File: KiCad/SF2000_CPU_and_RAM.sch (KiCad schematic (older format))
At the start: 5 parts, among them U10 IS61WV20488FBLL-10TLI, U11 IS61WV20488FBLL-10TLI, U12 IS61WV20488FBLL-10TLI, U8 68000D, U9 IS61WV20488FBLL-10TLI

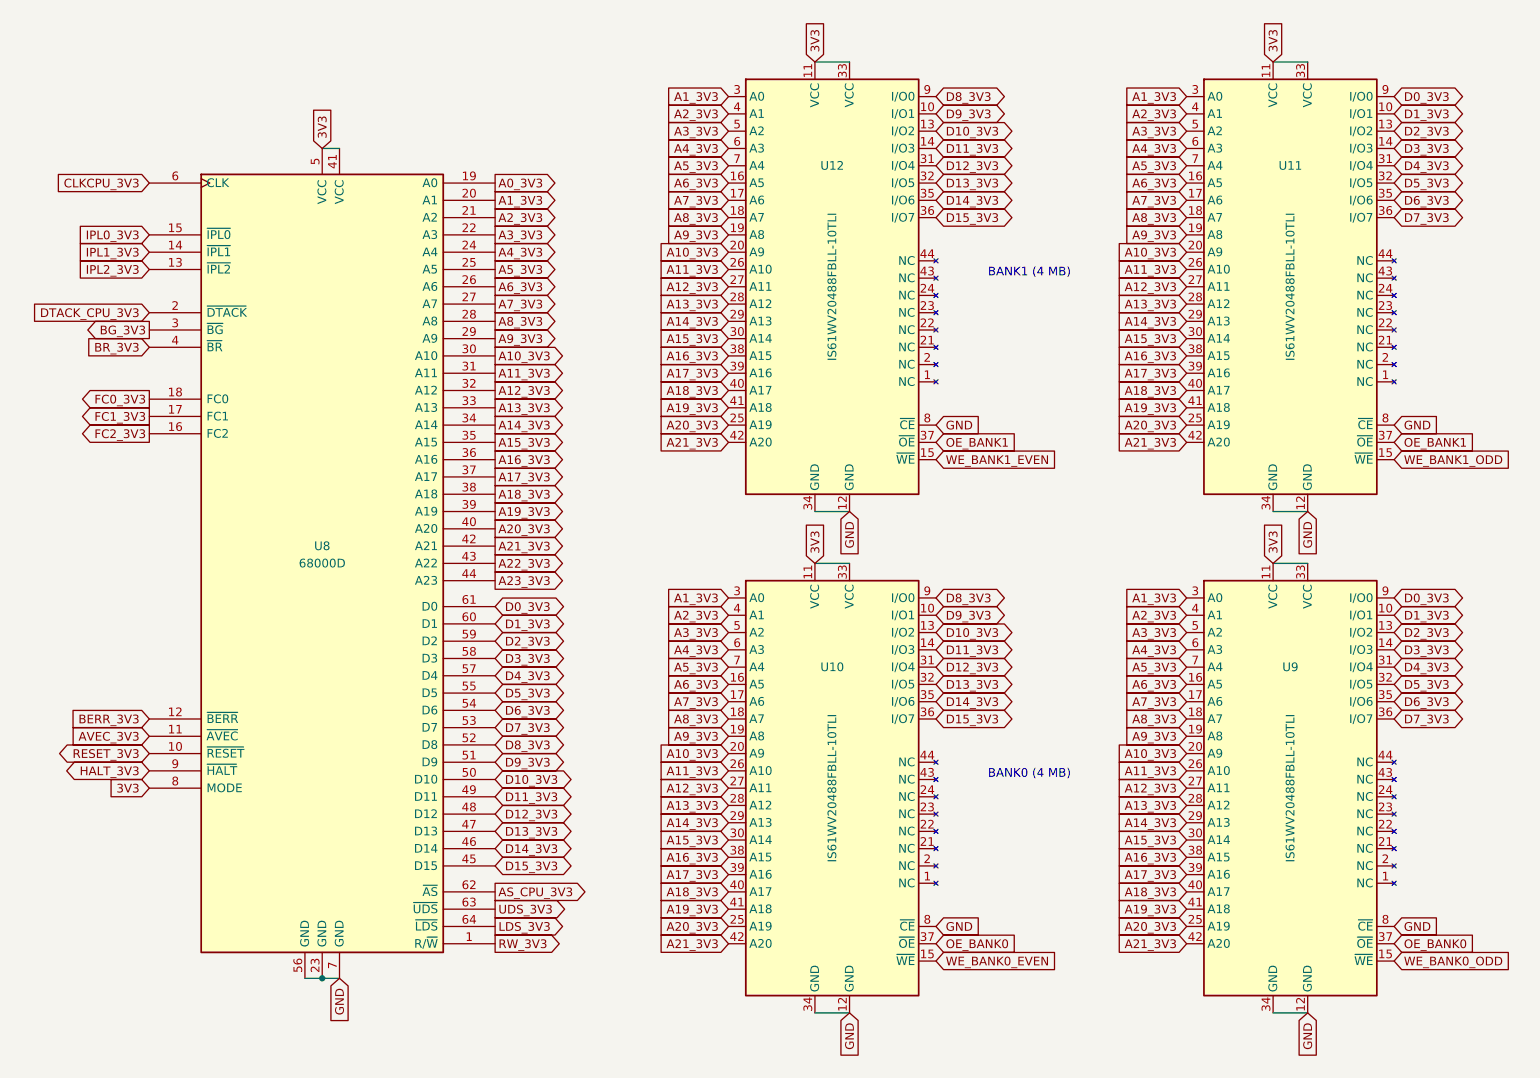
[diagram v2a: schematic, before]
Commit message: rotated SRAM footprints and routed a lot
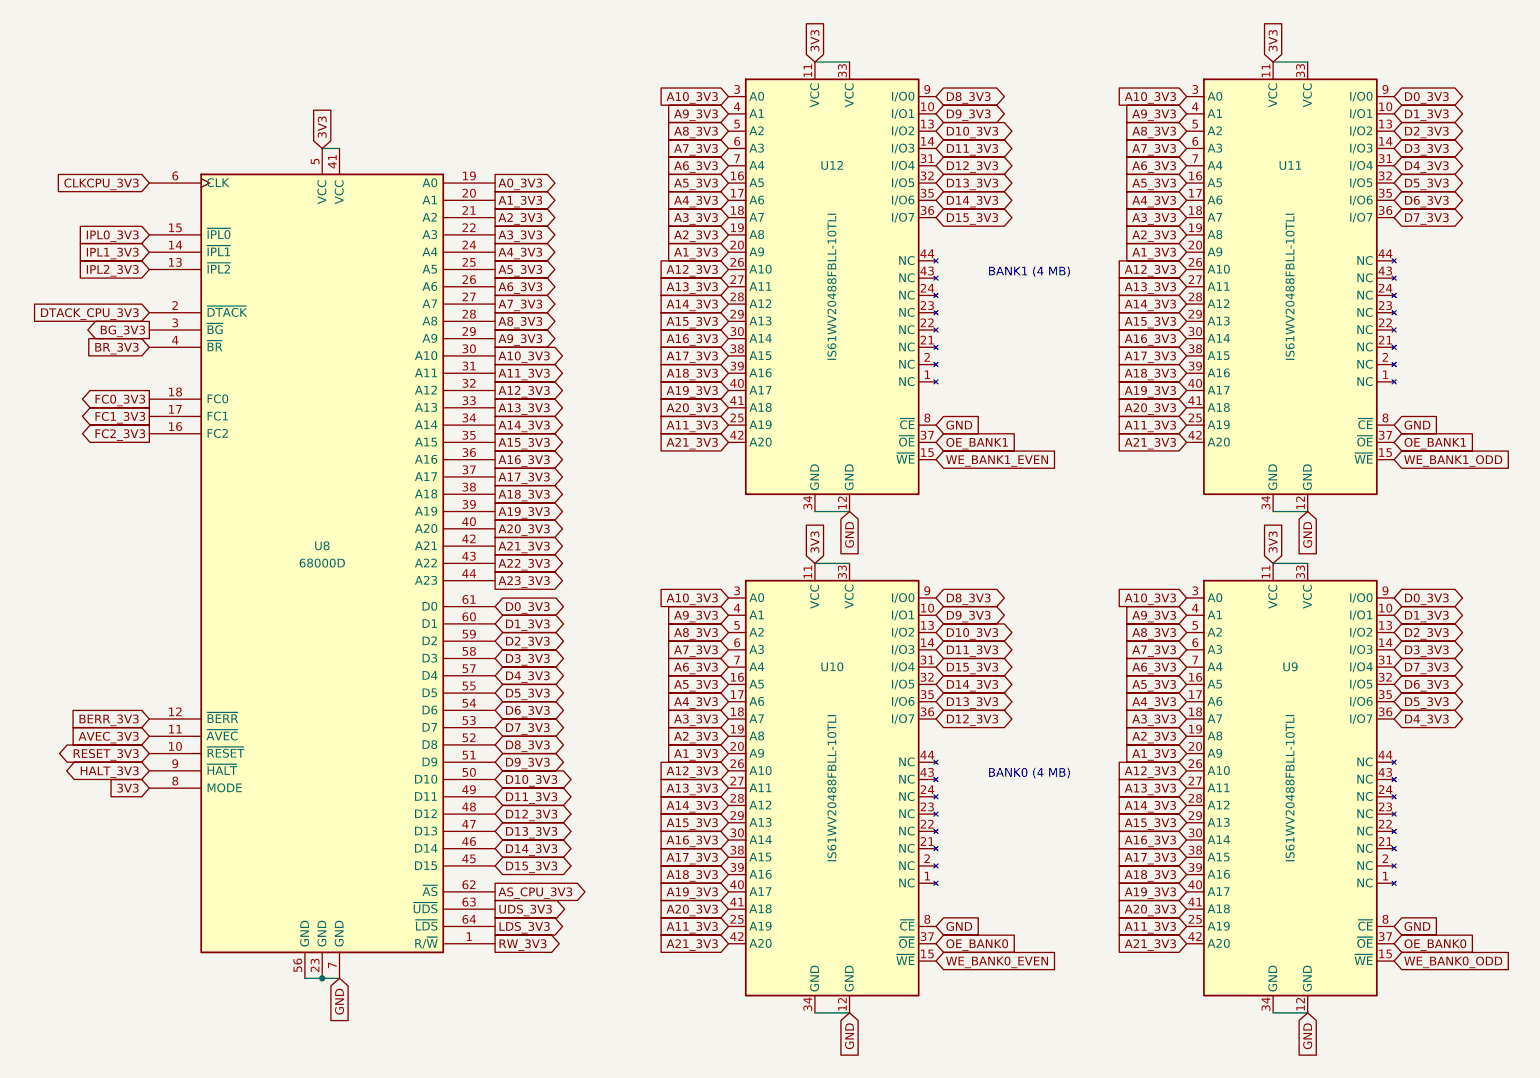
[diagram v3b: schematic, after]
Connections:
- net A10_3V3: now also U10.3 (A0), U11.3 (A0), U12.3 (A0), U9.3 (A0); no longer U10.20 (A9), U11.20 (A9), U12.20 (A9), U9.20 (A9)
- net A11_3V3: now also U10.25 (A19), U11.25 (A19), U12.25 (A19), U9.25 (A19); no longer U10.26 (A10), U11.26 (A10), U12.26 (A10), U9.26 (A10)
- net A12_3V3: now also U10.26 (A10), U11.26 (A10), U12.26 (A10), U9.26 (A10); no longer U10.27 (A11), U11.27 (A11), U12.27 (A11), U9.27 (A11)
- net A13_3V3: now also U10.27 (A11), U11.27 (A11), U12.27 (A11), U9.27 (A11); no longer U10.28 (A12), U11.28 (A12), U12.28 (A12), U9.28 (A12)
- net A14_3V3: now also U10.28 (A12), U11.28 (A12), U12.28 (A12), U9.28 (A12); no longer U10.29 (A13), U11.29 (A13), U12.29 (A13), U9.29 (A13)
- net A15_3V3: now also U10.29 (A13), U11.29 (A13), U12.29 (A13), U9.29 (A13); no longer U10.30 (A14), U11.30 (A14), U12.30 (A14), U9.30 (A14)
- net A16_3V3: now also U10.30 (A14), U11.30 (A14), U12.30 (A14), U9.30 (A14); no longer U10.38 (A15), U11.38 (A15), U12.38 (A15), U9.38 (A15)
- net A17_3V3: now also U10.38 (A15), U11.38 (A15), U12.38 (A15), U9.38 (A15); no longer U10.39 (A16), U11.39 (A16), U12.39 (A16), U9.39 (A16)
- net A18_3V3: now also U10.39 (A16), U11.39 (A16), U12.39 (A16), U9.39 (A16); no longer U10.40 (A17), U11.40 (A17), U12.40 (A17), U9.40 (A17)
- net A19_3V3: now also U10.40 (A17), U11.40 (A17), U12.40 (A17), U9.40 (A17); no longer U10.41 (A18), U11.41 (A18), U12.41 (A18), U9.41 (A18)
- net A1_3V3: now also U10.20 (A9), U11.20 (A9), U12.20 (A9), U9.20 (A9); no longer U10.3 (A0), U11.3 (A0), U12.3 (A0), U9.3 (A0)
- net A20_3V3: now also U10.41 (A18), U11.41 (A18), U12.41 (A18), U9.41 (A18); no longer U10.25 (A19), U11.25 (A19), U12.25 (A19), U9.25 (A19)
- net A2_3V3: now also U10.19 (A8), U11.19 (A8), U12.19 (A8), U9.19 (A8); no longer U10.4 (A1), U11.4 (A1), U12.4 (A1), U9.4 (A1)
- net A3_3V3: now also U10.18 (A7), U11.18 (A7), U12.18 (A7), U9.18 (A7); no longer U10.5 (A2), U11.5 (A2), U12.5 (A2), U9.5 (A2)
- net A4_3V3: now also U10.17 (A6), U11.17 (A6), U12.17 (A6), U9.17 (A6); no longer U10.6 (A3), U11.6 (A3), U12.6 (A3), U9.6 (A3)
- net A5_3V3: now also U10.16 (A5), U11.16 (A5), U12.16 (A5), U9.16 (A5); no longer U10.7 (A4), U11.7 (A4), U12.7 (A4), U9.7 (A4)
- net A6_3V3: now also U10.7 (A4), U11.7 (A4), U12.7 (A4), U9.7 (A4); no longer U10.16 (A5), U11.16 (A5), U12.16 (A5), U9.16 (A5)
- net A7_3V3: now also U10.6 (A3), U11.6 (A3), U12.6 (A3), U9.6 (A3); no longer U10.17 (A6), U11.17 (A6), U12.17 (A6), U9.17 (A6)
- net A8_3V3: now also U10.5 (A2), U11.5 (A2), U12.5 (A2), U9.5 (A2); no longer U10.18 (A7), U11.18 (A7), U12.18 (A7), U9.18 (A7)
- net A9_3V3: now also U10.4 (A1), U11.4 (A1), U12.4 (A1), U9.4 (A1); no longer U10.19 (A8), U11.19 (A8), U12.19 (A8), U9.19 (A8)
- net D12_3V3: now also U10.36 (I/O7); no longer U10.31 (I/O4)
- net D13_3V3: now also U10.35 (I/O6); no longer U10.32 (I/O5)
- net D14_3V3: now also U10.32 (I/O5); no longer U10.35 (I/O6)
- net D15_3V3: now also U10.31 (I/O4); no longer U10.36 (I/O7)
- net D4_3V3: now also U9.36 (I/O7); no longer U9.31 (I/O4)
- net D5_3V3: now also U9.35 (I/O6); no longer U9.32 (I/O5)
- net D6_3V3: now also U9.32 (I/O5); no longer U9.35 (I/O6)
- net D7_3V3: now also U9.31 (I/O4); no longer U9.36 (I/O7)
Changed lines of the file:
@@
 Text GLabel 8700 4200 2    50   BiDi ~ 0
 D3_3V3
+Text GLabel 8700 4600 2    50   BiDi ~ 0
+D4_3V3
+Text GLabel 8700 4500 2    50   BiDi ~ 0
+D5_3V3
+Text GLabel 8700 4400 2    50   BiDi ~ 0
+D6_3V3
 Text GLabel 8700 4300 2    50   BiDi ~ 0
-D4_3V3
-Text GLabel 8700 4400 2    50   BiDi ~ 0
-D5_3V3
-Text GLabel 8700 4500 2    50   BiDi ~ 0
-D6_3V3
-Text GLabel 8700 4600 2    50   BiDi ~ 0
 D7_3V3
 Text GLabel 6050 3900 2    50   BiDi ~ 0
@@
 Text GLabel 6050 4200 2    50   BiDi ~ 0
 D11_3V3
+Text GLabel 6050 4600 2    50   BiDi ~ 0
+D12_3V3
+Text GLabel 6050 4500 2    50   BiDi ~ 0
+D13_3V3
+Text GLabel 6050 4400 2    50   BiDi ~ 0
+D14_3V3
 Text GLabel 6050 4300 2    50   BiDi ~ 0
-D12_3V3
-Text GLabel 6050 4400 2    50   BiDi ~ 0
-D13_3V3
-Text GLabel 6050 4500 2    50   BiDi ~ 0
-D14_3V3
-Text GLabel 6050 4600 2    50   BiDi ~ 0
 D15_3V3
 Text GLabel 6050 1000 2    50   BiDi ~ 0
@@
 Text GLabel 6050 1700 2    50   BiDi ~ 0
 D15_3V3
+Text GLabel 4850 1900 0    50   Input ~ 0
+A1_3V3
+Text GLabel 4850 1800 0    50   Input ~ 0
+A2_3V3
+Text GLabel 4850 1700 0    50   Input ~ 0
+A3_3V3
+Text GLabel 4850 1600 0    50   Input ~ 0
+A4_3V3
+Text GLabel 4850 1500 0    50   Input ~ 0
+A5_3V3
+Text GLabel 4850 1400 0    50   Input ~ 0
+A6_3V3
+Text GLabel 4850 1300 0    50   Input ~ 0
+A7_3V3
+Text GLabel 4850 1200 0    50   Input ~ 0
+A8_3V3
+Text GLabel 4850 1100 0    50   Input ~ 0
+A9_3V3
 Text GLabel 4850 1000 0    50   Input ~ 0
-A1_3V3
-Text GLabel 4850 1100 0    50   Input ~ 0
-A2_3V3
-Text GLabel 4850 1200 0    50   Input ~ 0
-A3_3V3
-Text GLabel 4850 1300 0    50   Input ~ 0
-A4_3V3
-Text GLabel 4850 1400 0    50   Input ~ 0
-A5_3V3
-Text GLabel 4850 1500 0    50   Input ~ 0
-A6_3V3
-Text GLabel 4850 1600 0    50   Input ~ 0
-A7_3V3
-Text GLabel 4850 1700 0    50   Input ~ 0
-A8_3V3
-Text GLabel 4850 1800 0    50   Input ~ 0
-A9_3V3
-Text GLabel 4850 1900 0    50   Input ~ 0
-A10_3V3
+A10_3V3
+Text GLabel 4850 2900 0    50   Input ~ 0
+A11_3V3
 Text GLabel 4850 2000 0    50   Input ~ 0
-A11_3V3
+A12_3V3
 Text GLabel 4850 2100 0    50   Input ~ 0
-A12_3V3
+A13_3V3
 Text GLabel 4850 2200 0    50   Input ~ 0
-A13_3V3
+A14_3V3
 Text GLabel 4850 2300 0    50   Input ~ 0
-A14_3V3
+A15_3V3
 Text GLabel 4850 2400 0    50   Input ~ 0
-A15_3V3
+A16_3V3
 Text GLabel 4850 2500 0    50   Input ~ 0
-A16_3V3
+A17_3V3
 Text GLabel 4850 2600 0    50   Input ~ 0
-A17_3V3
+A18_3V3
 Text GLabel 4850 2700 0    50   Input ~ 0
-A18_3V3
+A19_3V3
 Text GLabel 4850 2800 0    50   Input ~ 0
-A19_3V3
-Text GLabel 4850 2900 0    50   Input ~ 0
 A20_3V3
 Text GLabel 4850 3000 0    50   Input ~ 0
 A21_3V3
+Text GLabel 7500 1900 0    50   Input ~ 0
+A1_3V3
+Text GLabel 7500 1800 0    50   Input ~ 0
+A2_3V3
+Text GLabel 7500 1700 0    50   Input ~ 0
+A3_3V3
+Text GLabel 7500 1600 0    50   Input ~ 0
+A4_3V3
+Text GLabel 7500 1500 0    50   Input ~ 0
+A5_3V3
+Text GLabel 7500 1400 0    50   Input ~ 0
+A6_3V3
+Text GLabel 7500 1300 0    50   Input ~ 0
+A7_3V3
+Text GLabel 7500 1200 0    50   Input ~ 0
+A8_3V3
+Text GLabel 7500 1100 0    50   Input ~ 0
+A9_3V3
 Text GLabel 7500 1000 0    50   Input ~ 0
-A1_3V3
-Text GLabel 7500 1100 0    50   Input ~ 0
-A2_3V3
-Text GLabel 7500 1200 0    50   Input ~ 0
-A3_3V3
-Text GLabel 7500 1300 0    50   Input ~ 0
-A4_3V3
-Text GLabel 7500 1400 0    50   Input ~ 0
-A5_3V3
-Text GLabel 7500 1500 0    50   Input ~ 0
-A6_3V3
-Text GLabel 7500 1600 0    50   Input ~ 0
-A7_3V3
-Text GLabel 7500 1700 0    50   Input ~ 0
-A8_3V3
-Text GLabel 7500 1800 0    50   Input ~ 0
-A9_3V3
-Text GLabel 7500 1900 0    50   Input ~ 0
-A10_3V3
+A10_3V3
+Text GLabel 4850 4800 0    50   Input ~ 0
+A1_3V3
+Text GLabel 4850 4700 0    50   Input ~ 0
+A2_3V3
+Text GLabel 4850 4600 0    50   Input ~ 0
+A3_3V3
+Text GLabel 4850 4500 0    50   Input ~ 0
+A4_3V3
+Text GLabel 4850 4400 0    50   Input ~ 0
+A5_3V3
+Text GLabel 4850 4300 0    50   Input ~ 0
+A6_3V3
+Text GLabel 4850 4200 0    50   Input ~ 0
+A7_3V3
+Text GLabel 4850 4100 0    50   Input ~ 0
+A8_3V3
+Text GLabel 4850 4000 0    50   Input ~ 0
+A9_3V3
+Text GLabel 4850 3900 0    50   Input ~ 0
+A10_3V3
+Text GLabel 7500 4800 0    50   Input ~ 0
+A1_3V3
+Text GLabel 7500 4700 0    50   Input ~ 0
+A2_3V3
+Text GLabel 7500 4600 0    50   Input ~ 0
+A3_3V3
+Text GLabel 7500 4500 0    50   Input ~ 0
+A4_3V3
+Text GLabel 7500 4400 0    50   Input ~ 0
+A5_3V3
+Text GLabel 7500 4300 0    50   Input ~ 0
+A6_3V3
+Text GLabel 7500 4200 0    50   Input ~ 0
+A7_3V3
+Text GLabel 7500 4100 0    50   Input ~ 0
+A8_3V3
+Text GLabel 7500 4000 0    50   Input ~ 0
+A9_3V3
+Text GLabel 7500 3900 0    50   Input ~ 0
+A10_3V3
+Text GLabel 7500 2900 0    50   Input ~ 0
+A11_3V3
 Text GLabel 7500 2000 0    50   Input ~ 0
-A11_3V3
+A12_3V3
 Text GLabel 7500 2100 0    50   Input ~ 0
-A12_3V3
+A13_3V3
 Text GLabel 7500 2200 0    50   Input ~ 0
-A13_3V3
+A14_3V3
 Text GLabel 7500 2300 0    50   Input ~ 0
-A14_3V3
+A15_3V3
 Text GLabel 7500 2400 0    50   Input ~ 0
-A15_3V3
+A16_3V3
 Text GLabel 7500 2500 0    50   Input ~ 0
-A16_3V3
+A17_3V3
 Text GLabel 7500 2600 0    50   Input ~ 0
-A17_3V3
+A18_3V3
 Text GLabel 7500 2700 0    50   Input ~ 0
-A18_3V3
+A19_3V3
 Text GLabel 7500 2800 0    50   Input ~ 0
-A19_3V3
-Text GLabel 7500 2900 0    50   Input ~ 0
 A20_3V3
 Text GLabel 7500 3000 0    50   Input ~ 0
 A21_3V3
-Text GLabel 7500 3900 0    50   Input ~ 0
-A1_3V3
-Text GLabel 7500 4000 0    50   Input ~ 0
-A2_3V3
-Text GLabel 7500 4100 0    50   Input ~ 0
-A3_3V3
-Text GLabel 7500 4200 0    50   Input ~ 0
-A4_3V3
-Text GLabel 7500 4300 0    50   Input ~ 0
-A5_3V3
-Text GLabel 7500 4400 0    50   Input ~ 0
-A6_3V3
-Text GLabel 7500 4500 0    50   Input ~ 0
-A7_3V3
-Text GLabel 7500 4600 0    50   Input ~ 0
-A8_3V3
-Text GLabel 7500 4700 0    50   Input ~ 0
-A9_3V3
-Text GLabel 7500 4800 0    50   Input ~ 0
-A10_3V3
+Text GLabel 7500 5800 0    50   Input ~ 0
+A11_3V3
 Text GLabel 7500 4900 0    50   Input ~ 0
-A11_3V3
+A12_3V3
 Text GLabel 7500 5000 0    50   Input ~ 0
-A12_3V3
+A13_3V3
 Text GLabel 7500 5100 0    50   Input ~ 0
-A13_3V3
+A14_3V3
 Text GLabel 7500 5200 0    50   Input ~ 0
-A14_3V3
+A15_3V3
 Text GLabel 7500 5300 0    50   Input ~ 0
-A15_3V3
+A16_3V3
 Text GLabel 7500 5400 0    50   Input ~ 0
-A16_3V3
+A17_3V3
 Text GLabel 7500 5500 0    50   Input ~ 0
-A17_3V3
+A18_3V3
 Text GLabel 7500 5600 0    50   Input ~ 0
-A18_3V3
+A19_3V3
 Text GLabel 7500 5700 0    50   Input ~ 0
-A19_3V3
-Text GLabel 7500 5800 0    50   Input ~ 0
 A20_3V3
 Text GLabel 7500 5900 0    50   Input ~ 0
 A21_3V3
-Text GLabel 4850 3900 0    50   Input ~ 0
-A1_3V3
-Text GLabel 4850 4000 0    50   Input ~ 0
-A2_3V3
-Text GLabel 4850 4100 0    50   Input ~ 0
-A3_3V3
-Text GLabel 4850 4200 0    50   Input ~ 0
-A4_3V3
-Text GLabel 4850 4300 0    50   Input ~ 0
-A5_3V3
-Text GLabel 4850 4400 0    50   Input ~ 0
-A6_3V3
-Text GLabel 4850 4500 0    50   Input ~ 0
-A7_3V3
-Text GLabel 4850 4600 0    50   Input ~ 0
-A8_3V3
-Text GLabel 4850 4700 0    50   Input ~ 0
-A9_3V3
-Text GLabel 4850 4800 0    50   Input ~ 0
-A10_3V3
+Text GLabel 4850 5800 0    50   Input ~ 0
+A11_3V3
 Text GLabel 4850 4900 0    50   Input ~ 0
-A11_3V3
+A12_3V3
 Text GLabel 4850 5000 0    50   Input ~ 0
-A12_3V3
+A13_3V3
 Text GLabel 4850 5100 0    50   Input ~ 0
-A13_3V3
+A14_3V3
 Text GLabel 4850 5200 0    50   Input ~ 0
-A14_3V3
+A15_3V3
 Text GLabel 4850 5300 0    50   Input ~ 0
-A15_3V3
+A16_3V3
 Text GLabel 4850 5400 0    50   Input ~ 0
-A16_3V3
+A17_3V3
 Text GLabel 4850 5500 0    50   Input ~ 0
-A17_3V3
+A18_3V3
 Text GLabel 4850 5600 0    50   Input ~ 0
-A18_3V3
+A19_3V3
 Text GLabel 4850 5700 0    50   Input ~ 0
-A19_3V3
-Text GLabel 4850 5800 0    50   Input ~ 0
 A20_3V3
 Text GLabel 4850 5900 0    50   Input ~ 0
